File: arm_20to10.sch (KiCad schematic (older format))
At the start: 2 parts

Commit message: - save
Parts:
- added P1, P2, P3: TST, ~, symbol TST
- gave numbers to parts that had none: 2
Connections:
- net VCC: now reaches J2.1 (VCC)
- net VCC: now also J1.1 (VTREF), J1.2 (VCC(optional)), P2.1
- net NRST: now reaches J2.10 (nRESET)
- net NRST: now also J1.15 (nRESET)
- net TMS/SWDIO: now reaches J2.2 (SWDIO/TMS)
- net TMS/SWDIO: now also J1.7 (SWDIO/TMS)
- net GND: now reaches J2.3 (GND)
- net GND: now also J1.10 (GND), J1.11 (RTCK), J1.12 (GND), J1.14 (GND), J1.16 (GND), J1.18 (GND), J1.20 (GND), J1.4 (GND), J1.6 (GND), J1.8 (GND), J2.5 (GND), J2.7 (RTCK), J2.9 (GND), P3.1
- net TCLK/SWCLK: now reaches J2.4 (SWCLK/TCLK)
- net TCLK/SWCLK: now also J1.9 (SWCLK/TCLK)
- net SWO/TDO: now reaches J2.6 (SWO/TDO)
- net SWO/TDO: now also J1.13 (SWO/TDO)
- net TDI: now reaches J2.8 (NC-EXTb/TDI)
- net TDI: now also J1.5 (TDI)
- net 5V: now reaches J1.19 (5V-SUPPLY)
- net 5V: now also P1.1
- net TRST: now reaches J1.3 (TRST)
- no-connect marks 0 -> 1
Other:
- moved on the sheet: J1, J2
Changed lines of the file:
@@
 Sheet 1 1
 Title ""
-Date "29 jan 2014"
+Date "30 jan 2014"
 Rev ""
 Comp ""
@@
 $EndDescr
 $Comp
-L ARM_10PIN J?
+L ARM_10PIN J2
 U 1 1 52E97CAC
-P 6450 3600
-F 0 "J?" H 6450 2600 60  0000 C CNN
-F 1 "ARM_10PIN" H 6450 4250 60  0000 C CNN
-F 2 "~" H 6450 3600 60  0000 C CNN
-F 3 "~" H 6450 3600 60  0000 C CNN
-	1    6450 3600
+P 6550 4250
+F 0 "J2" H 6550 3250 60  0000 C CNN
+F 1 "ARM_10PIN" H 6550 4900 60  0000 C CNN
+F 2 "~" H 6550 4250 60  0000 C CNN
+F 3 "~" H 6550 4250 60  0000 C CNN
+	1    6550 4250
 	-1   0    0    -1
 $EndComp
 $Comp
-L ARM_20PIN J?
+L ARM_20PIN J1
 U 1 1 52E9849C
-P 3750 3350
-F 0 "J?" H 3750 1600 60  0000 C CNN
-F 1 "ARM_20PIN" H 3750 4750 60  0000 C CNN
-F 2 "~" H 3750 3350 60  0000 C CNN
-F 3 "~" H 3750 3350 60  0000 C CNN
-	1    3750 3350
-	1    0    0    -1
-$EndComp
+P 3400 3500
+F 0 "J1" H 3400 1750 60  0000 C CNN
+F 1 "ARM_20PIN" H 3400 4900 60  0000 C CNN
+F 2 "~" H 3400 3500 60  0000 C CNN
+F 3 "~" H 3400 3500 60  0000 C CNN
+	1    3400 3500
+	1    0    0    -1
+$EndComp
+Text GLabel 3950 3150 2    60   Input ~ 0
+TMS/SWDIO
+Text GLabel 3950 3450 2    60   Input ~ 0
+TCLK/SWCLK
+Text GLabel 3950 4050 2    60   Input ~ 0
+SWO/TDO
+Text GLabel 3950 4350 2    60   Input ~ 0
+NRST
+Wire Wire Line
+	3950 3150 3850 3150
+Wire Wire Line
+	3950 3450 3850 3450
+Wire Wire Line
+	3950 4050 3850 4050
+Wire Wire Line
+	3950 4350 3850 4350
+Text GLabel 3950 2850 2    60   Input ~ 0
+TDI
+Wire Wire Line
+	3950 2850 3850 2850
+Text GLabel 3950 2550 2    60   Input ~ 0
+TRST
+Wire Wire Line
+	3950 2550 3850 2550
+$Comp
+L GND #PWR01
+U 1 1 52E99F2E
+P 4000 5200
+F 0 "#PWR01" H 4000 5200 30  0001 C CNN
+F 1 "GND" H 4000 5130 30  0001 C CNN
+F 2 "" H 4000 5200 60  0000 C CNN
+F 3 "" H 4000 5200 60  0000 C CNN
+	1    4000 5200
+	1    0    0    -1
+$EndComp
+Wire Wire Line
+	4000 2700 4000 5200
+Wire Wire Line
+	4000 5100 3900 5100
+Wire Wire Line
+	3900 4800 4000 4800
+Connection ~ 4000 5100
+Wire Wire Line
+	3900 4500 4000 4500
+Connection ~ 4000 4800
+Wire Wire Line
+	3900 4200 4000 4200
+Connection ~ 4000 4500
+Wire Wire Line
+	3900 3900 4000 3900
+Connection ~ 4000 4200
+Wire Wire Line
+	3900 3600 4000 3600
+Connection ~ 4000 3900
+Wire Wire Line
+	3900 3300 4000 3300
+Connection ~ 4000 3600
+Wire Wire Line
+	3900 3000 4000 3000
+Connection ~ 4000 3300
+Wire Wire Line
+	3900 2700 4000 2700
+Connection ~ 4000 3000
+Text GLabel 3950 3750 2    60   Input ~ 0
+RTCK
+Wire Wire Line
+	3950 3750 3850 3750
+Wire Wire Line
+	6000 4650 6100 4650
+Text GLabel 6000 4650 0    60   Input ~ 0
+RTCK
+Text GLabel 5950 5100 0    60   Input ~ 0
+NRST
+Wire Wire Line
+	5950 5100 6050 5100
+$Comp
+L GND #PWR02
+U 1 1 52E9A0B6
+P 6000 4950
+F 0 "#PWR02" H 6000 4950 30  0001 C CNN
+F 1 "GND" H 6000 4880 30  0001 C CNN
+F 2 "" H 6000 4950 60  0000 C CNN
+F 3 "" H 6000 4950 60  0000 C CNN
+	1    6000 4950
+	1    0    0    -1
+$EndComp
+Wire Wire Line
+	6000 4950 6100 4950
+Wire Wire Line
+	6100 4350 6000 4350
+Wire Wire Line
+	6000 4050 6000 4950
+Wire Wire Line
+	6100 4050 6000 4050
+Connection ~ 6000 4350
+Text GLabel 5950 3900 0    60   Input ~ 0
+TMS/SWDIO
+Wire Wire Line
+	5950 3900 6050 3900
+Text GLabel 5950 4200 0    60   Input ~ 0
+TCLK/SWCLK
+Wire Wire Line
+	5950 4200 6050 4200
+Text GLabel 5950 4500 0    60   Input ~ 0
+SWO/TDO
+Wire Wire Line
+	6050 4500 5950 4500
+Text GLabel 5950 4800 0    60   Input ~ 0
+TDI
+Wire Wire Line
+	5950 4800 6050 4800
+$Comp
+L TST P1
+U 1 1 52E9A2C6
+P 5600 2700
+F 0 "P1" H 5600 3000 40  0000 C CNN
+F 1 "TST" H 5600 2950 30  0000 C CNN
+F 2 "~" H 5600 2700 60  0000 C CNN
+F 3 "~" H 5600 2700 60  0000 C CNN
+	1    5600 2700
+	1    0    0    -1
+$EndComp
+Text GLabel 3950 4950 2    60   Input ~ 0
+5V
+Wire Wire Line
+	3950 4950 3850 4950
+Text GLabel 6000 3750 0    60   Input ~ 0
+VCC
+Wire Wire Line
+	6100 3750 6000 3750
+Text GLabel 4100 2400 2    60   Input ~ 0
+VCC
+Wire Wire Line
+	3900 2400 4100 2400
+Wire Wire Line
+	4000 2400 4000 2250
+Wire Wire Line
+	4000 2250 3850 2250
+Connection ~ 4000 2400
+NoConn ~ 3850 4650
+Text GLabel 5750 2800 3    60   Input ~ 0
+VCC
+$Comp
+L TST P2
+U 1 1 52E9A439
+P 5750 2700
+F 0 "P2" H 5750 3000 40  0000 C CNN
+F 1 "TST" H 5750 2950 30  0000 C CNN
+F 2 "~" H 5750 2700 60  0000 C CNN
+F 3 "~" H 5750 2700 60  0000 C CNN
+	1    5750 2700
+	1    0    0    -1
+$EndComp
+Text GLabel 5600 2800 3    60   Input ~ 0
+5V
+Wire Wire Line
+	5600 2800 5600 2700
+Wire Wire Line
+	5750 2700 5750 2800
+$Comp
+L GND #PWR03
+U 1 1 52E9A4EA
+P 5900 2800
+F 0 "#PWR03" H 5900 2800 30  0001 C CNN
+F 1 "GND" H 5900 2730 30  0001 C CNN
+F 2 "" H 5900 2800 60  0000 C CNN
+F 3 "" H 5900 2800 60  0000 C CNN
+	1    5900 2800
+	1    0    0    -1
+$EndComp
+$Comp
+L TST P3
+U 1 1 52E9A4F0
+P 5900 2700
+F 0 "P3" H 5900 3000 40  0000 C CNN
+F 1 "TST" H 5900 2950 30  0000 C CNN
+F 2 "~" H 5900 2700 60  0000 C CNN
+F 3 "~" H 5900 2700 60  0000 C CNN
+	1    5900 2700
+	1    0    0    -1
+$EndComp
+Wire Wire Line
+	5900 2700 5900 2800
 $EndSCHEMATC

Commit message: - start layout
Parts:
- P1: value TST -> +5V
- P2: value TST -> VCC
- P3: value TST -> GND
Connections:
- net GND: no longer J1.11 (RTCK), J2.7 (RTCK)
- new net RTCK: J1.11 (RTCK), J2.7 (RTCK)
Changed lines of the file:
@@
 Text GLabel 3950 3150 2    60   Input ~ 0
 TMS/SWDIO
-Text GLabel 3950 3450 2    60   Input ~ 0
-TCLK/SWCLK
 Text GLabel 3950 4050 2    60   Input ~ 0
 SWO/TDO
@@
 $EndComp
 Wire Wire Line
-	4000 2700 4000 5200
+	4000 2700 4000 3000
+Wire Wire Line
+	4000 3000 4000 3300
+Wire Wire Line
+	4000 3300 4000 3600
+Wire Wire Line
+	4000 3600 4000 3900
+Wire Wire Line
+	4000 3900 4000 4200
+Wire Wire Line
+	4000 4200 4000 4500
+Wire Wire Line
+	4000 4500 4000 4800
+Wire Wire Line
+	4000 4800 4000 5100
+Wire Wire Line
+	4000 5100 4000 5200
 Wire Wire Line
 	4000 5100 3900 5100
@@
 	3900 2700 4000 2700
 Connection ~ 4000 3000
-Text GLabel 3950 3750 2    60   Input ~ 0
-RTCK
 Wire Wire Line
 	3950 3750 3850 3750
 Wire Wire Line
 	6000 4650 6100 4650
-Text GLabel 6000 4650 0    60   Input ~ 0
-RTCK
 Text GLabel 5950 5100 0    60   Input ~ 0
 NRST
@@
 	6100 4350 6000 4350
 Wire Wire Line
-	6000 4050 6000 4950
-Wire Wire Line
 	6100 4050 6000 4050
-Connection ~ 6000 4350
 Text GLabel 5950 3900 0    60   Input ~ 0
 TMS/SWDIO
 Wire Wire Line
 	5950 3900 6050 3900
-Text GLabel 5950 4200 0    60   Input ~ 0
-TCLK/SWCLK
 Wire Wire Line
 	5950 4200 6050 4200
@@
 P 5600 2700
 F 0 "P1" H 5600 3000 40  0000 C CNN
-F 1 "TST" H 5600 2950 30  0000 C CNN
+F 1 "+5V" H 5600 2950 30  0000 C CNN
 F 2 "~" H 5600 2700 60  0000 C CNN
 F 3 "~" H 5600 2700 60  0000 C CNN
@@
 VCC
 Wire Wire Line
-	3900 2400 4100 2400
+	3900 2400 4000 2400
+Wire Wire Line
+	4000 2400 4100 2400
 Wire Wire Line
 	4000 2400 4000 2250
@@
 P 5750 2700
 F 0 "P2" H 5750 3000 40  0000 C CNN
-F 1 "TST" H 5750 2950 30  0000 C CNN
+F 1 "VCC" H 5750 2950 30  0000 C CNN
 F 2 "~" H 5750 2700 60  0000 C CNN
 F 3 "~" H 5750 2700 60  0000 C CNN
@@
 P 5900 2700
 F 0 "P3" H 5900 3000 40  0000 C CNN
-F 1 "TST" H 5900 2950 30  0000 C CNN
+F 1 "GND" H 5900 2950 30  0000 C CNN
 F 2 "~" H 5900 2700 60  0000 C CNN
 F 3 "~" H 5900 2700 60  0000 C CNN
@@
 Wire Wire Line
 	5900 2700 5900 2800
+Text GLabel 3950 3750 2    60   Input ~ 0
+RTCK
+Text GLabel 6000 4650 0    60   Input ~ 0
+RTCK
+$Comp
+L GND #PWR04
+U 1 1 52E9A6FB
+P 6000 4350
+F 0 "#PWR04" H 6000 4350 30  0001 C CNN
+F 1 "GND" H 6000 4280 30  0001 C CNN
+F 2 "" H 6000 4350 60  0000 C CNN
+F 3 "" H 6000 4350 60  0000 C CNN
+	1    6000 4350
+	1    0    0    -1
+$EndComp
+Text GLabel 3950 3450 2    60   Input ~ 0
+TCLK/SWCLK
+Text GLabel 5950 4200 0    60   Input ~ 0
+TCLK/SWCLK
+$Comp
+L GND #PWR05
+U 1 1 52E9A838
+P 6000 4050
+F 0 "#PWR05" H 6000 4050 30  0001 C CNN
+F 1 "GND" H 6000 3980 30  0001 C CNN
+F 2 "" H 6000 4050 60  0000 C CNN
+F 3 "" H 6000 4050 60  0000 C CNN
+	1    6000 4050
+	1    0    0    -1
+$EndComp
 $EndSCHEMATC

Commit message: - add gerbers, finish layout
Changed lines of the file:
@@
 $EndComp
 Wire Wire Line
-	4000 2700 4000 3000
-Wire Wire Line
-	4000 3000 4000 3300
-Wire Wire Line
-	4000 3300 4000 3600
-Wire Wire Line
-	4000 3600 4000 3900
-Wire Wire Line
-	4000 3900 4000 4200
-Wire Wire Line
-	4000 4200 4000 4500
-Wire Wire Line
-	4000 4500 4000 4800
-Wire Wire Line
-	4000 4800 4000 5100
-Wire Wire Line
-	4000 5100 4000 5200
+	4000 2700 4000 5200
 Wire Wire Line
 	4000 5100 3900 5100
@@
 VCC
 Wire Wire Line
-	3900 2400 4000 2400
-Wire Wire Line
-	4000 2400 4100 2400
+	3900 2400 4100 2400
 Wire Wire Line
 	4000 2400 4000 2250

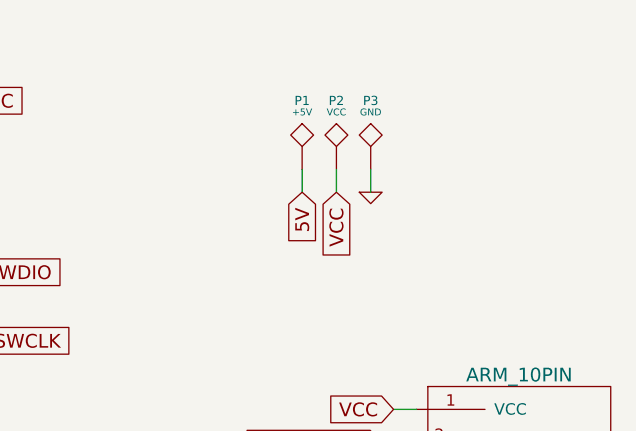
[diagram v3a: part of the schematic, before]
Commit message: - layout done. add gnd next to vcc test point.
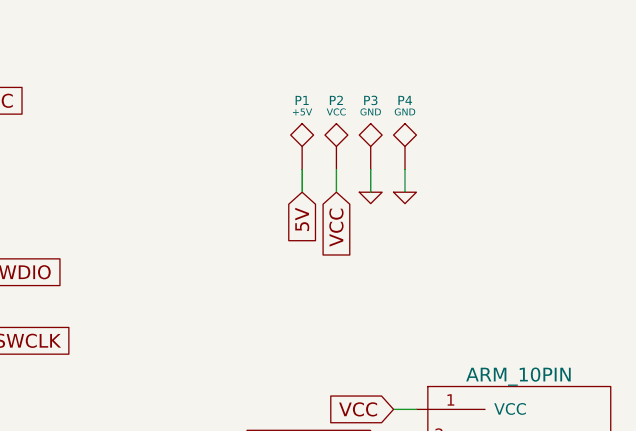
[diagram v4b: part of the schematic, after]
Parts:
- added P4: GND, ~, symbol TST
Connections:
- net GND: now also P4.1
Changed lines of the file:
@@
 Sheet 1 1
 Title ""
-Date "30 jan 2014"
+Date "31 jan 2014"
 Rev ""
 Comp ""
@@
 	1    0    0    -1
 $EndComp
+$Comp
+L GND #PWR06
+U 1 1 52EBCB6E
+P 6050 2800
+F 0 "#PWR06" H 6050 2800 30  0001 C CNN
+F 1 "GND" H 6050 2730 30  0001 C CNN
+F 2 "" H 6050 2800 60  0000 C CNN
+F 3 "" H 6050 2800 60  0000 C CNN
+	1    6050 2800
+	1    0    0    -1
+$EndComp
+$Comp
+L TST P4
+U 1 1 52EBCB74
+P 6050 2700
+F 0 "P4" H 6050 3000 40  0000 C CNN
+F 1 "GND" H 6050 2950 30  0000 C CNN
+F 2 "~" H 6050 2700 60  0000 C CNN
+F 3 "~" H 6050 2700 60  0000 C CNN
+	1    6050 2700
+	1    0    0    -1
+$EndComp
+Wire Wire Line
+	6050 2700 6050 2800
 $EndSCHEMATC

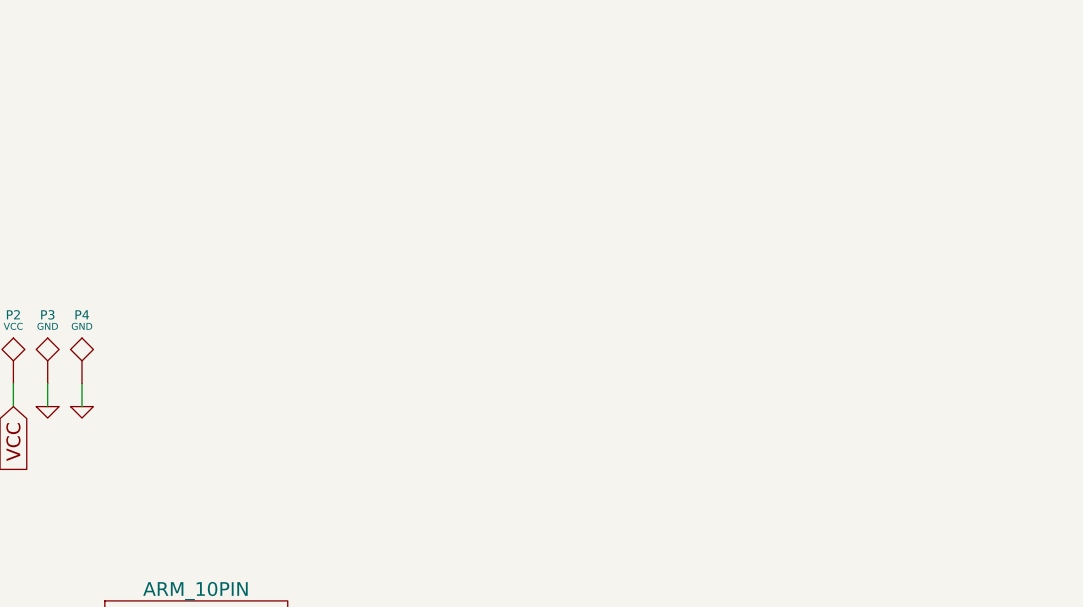
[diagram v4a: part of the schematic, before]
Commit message: - add 3.3v supply option
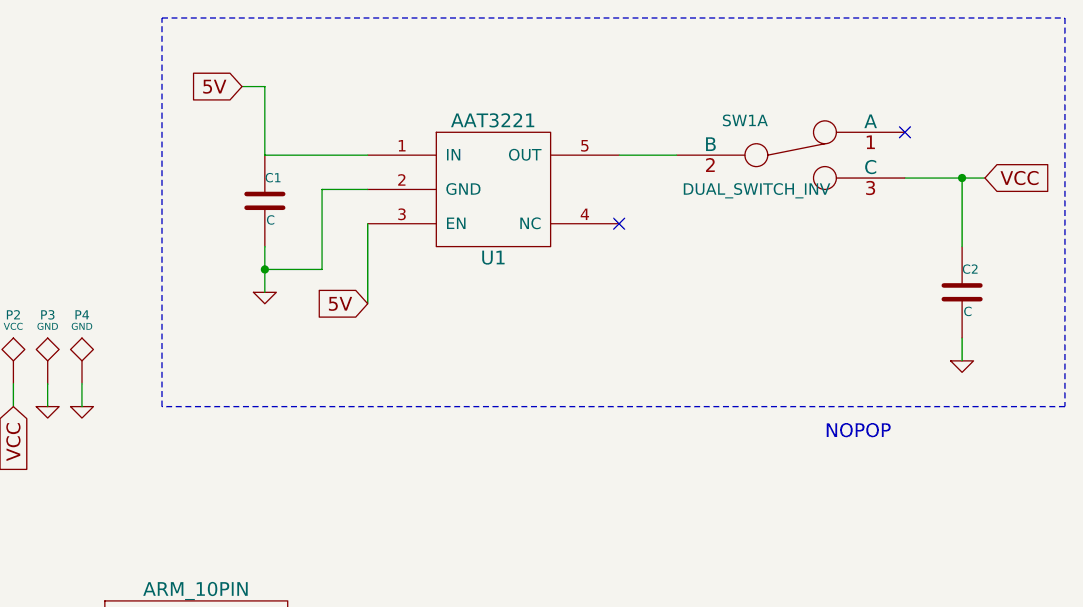
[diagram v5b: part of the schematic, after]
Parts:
- added C1, C2: C, ~, symbol C
- added SW1: DUAL_SWITCH_INV, ~, symbol DUAL_SWITCH_INV
- added U1: AAT3221, symbol AAT3221
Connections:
- net 5V: now also C1.1, U1.1 (IN), U1.3 (EN)
- net GND: now also C1.2, C2.2, U1.2 (GND)
- net VCC: now also C2.1, SW1.3 (C)
- new net: SW1.2 (B), U1.5 (OUT)
- no-connect marks 1 -> 3
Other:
- note added: "NOPOP"
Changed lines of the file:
@@
 Sheet 1 1
 Title ""
-Date "31 jan 2014"
+Date "13 feb 2014"
 Rev ""
 Comp ""
@@
 Wire Wire Line
 	6050 2700 6050 2800
+$Comp
+L AAT3221 U1
+U 1 1 52FC2F3B
+P 7850 1950
+F 0 "U1" H 7850 1750 60  0000 C CNN
+F 1 "AAT3221" H 7850 2350 60  0000 C CNN
+F 2 "" H 7850 1950 60  0000 C CNN
+F 3 "" H 7850 1950 60  0000 C CNN
+	1    7850 1950
+	1    0    0    -1
+$EndComp
+$Comp
+L C C2
+U 1 1 52FC3072
+P 9900 2300
+F 0 "C2" H 9900 2400 40  0000 L CNN
+F 1 "C" H 9906 2215 40  0000 L CNN
+F 2 "~" H 9938 2150 30  0000 C CNN
+F 3 "~" H 9900 2300 60  0000 C CNN
+	1    9900 2300
+	1    0    0    -1
+$EndComp
+NoConn ~ 8400 2000
+$Comp
+L C C1
+U 1 1 52FC308F
+P 6850 1900
+F 0 "C1" H 6850 2000 40  0000 L CNN
+F 1 "C" H 6856 1815 40  0000 L CNN
+F 2 "~" H 6888 1750 30  0000 C CNN
+F 3 "~" H 6850 1900 60  0000 C CNN
+	1    6850 1900
+	1    0    0    -1
+$EndComp
+Text GLabel 6750 1400 0    60   Input ~ 0
+5V
+Wire Wire Line
+	6750 1400 6850 1400
+Wire Wire Line
+	6850 1400 6850 1700
+Wire Wire Line
+	6850 1700 7300 1700
+$Comp
+L GND #PWR07
+U 1 1 52FC3225
+P 6850 2300
+F 0 "#PWR07" H 6850 2300 30  0001 C CNN
+F 1 "GND" H 6850 2230 30  0001 C CNN
+F 2 "" H 6850 2300 60  0000 C CNN
+F 3 "" H 6850 2300 60  0000 C CNN
+	1    6850 2300
+	1    0    0    -1
+$EndComp
+Wire Wire Line
+	7100 1850 7100 2200
+Wire Wire Line
+	7100 1850 7300 1850
+Wire Wire Line
+	6850 2100 6850 2300
+Wire Wire Line
+	7100 2200 6850 2200
+Connection ~ 6850 2200
+Text GLabel 7300 2350 0    60   Input ~ 0
+5V
+Wire Wire Line
+	7300 2000 7300 2350
+$Comp
+L GND #PWR08
+U 1 1 52FC3410
+P 9900 2600
+F 0 "#PWR08" H 9900 2600 30  0001 C CNN
+F 1 "GND" H 9900 2530 30  0001 C CNN
+F 2 "" H 9900 2600 60  0000 C CNN
+F 3 "" H 9900 2600 60  0000 C CNN
+	1    9900 2600
+	1    0    0    -1
+$EndComp
+Wire Wire Line
+	9900 2600 9900 2500
+Text GLabel 10000 1800 2    60   Input ~ 0
+VCC
+Wire Wire Line
+	9650 1800 10000 1800
+Wire Wire Line
+	9900 1800 9900 2100
+$Comp
+L DUAL_SWITCH_INV SW1
+U 1 1 52FC3911
+P 9150 1700
+F 0 "SW1" H 8950 1850 50  0000 C CNN
+F 1 "DUAL_SWITCH_INV" H 9000 1550 50  0000 C CNN
+F 2 "~" H 9150 1700 60  0000 C CNN
+F 3 "~" H 9150 1700 60  0000 C CNN
+	1    9150 1700
+	1    0    0    -1
+$EndComp
+NoConn ~ 9650 1600
+Wire Wire Line
+	8650 1700 8400 1700
+Connection ~ 9900 1800
+Wire Notes Line
+	6400 1100 10350 1100
+Wire Notes Line
+	10350 1100 10350 2800
+Wire Notes Line
+	10350 2800 6400 2800
+Wire Notes Line
+	6400 2800 6400 1100
+Text Notes 9300 2950 0    60   ~ 0
+NOPOP
 $EndSCHEMATC

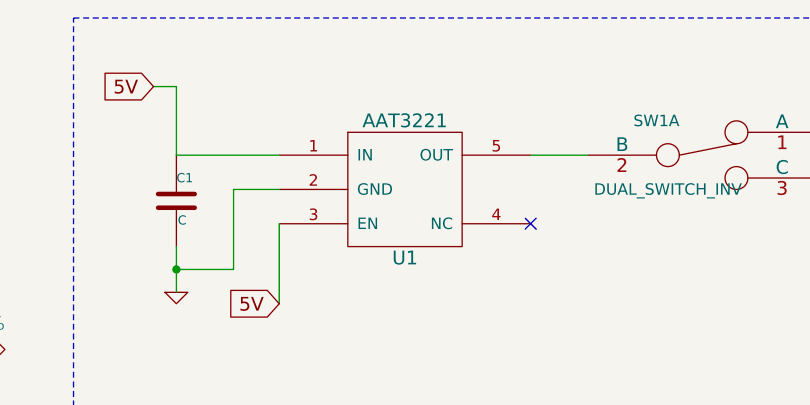
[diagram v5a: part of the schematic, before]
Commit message: - add comp. associations for ldo + switch
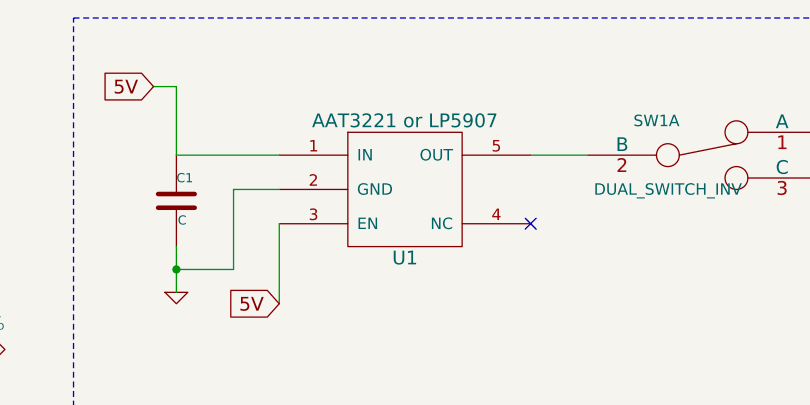
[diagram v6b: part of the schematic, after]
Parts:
- U1: value AAT3221 -> AAT3221 or LP5907
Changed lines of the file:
@@
 Sheet 1 1
 Title ""
-Date "13 feb 2014"
+Date "20 feb 2014"
 Rev ""
 Comp ""
@@
 P 7850 1950
 F 0 "U1" H 7850 1750 60  0000 C CNN
-F 1 "AAT3221" H 7850 2350 60  0000 C CNN
+F 1 "AAT3221 or LP5907" H 7850 2350 60  0000 C CNN
 F 2 "" H 7850 1950 60  0000 C CNN
 F 3 "" H 7850 1950 60  0000 C CNN
